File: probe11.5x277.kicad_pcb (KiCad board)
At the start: 2 copper layers, 297 x 11.5 mm, 12 parts, among them J1 CN10, J2 CN10

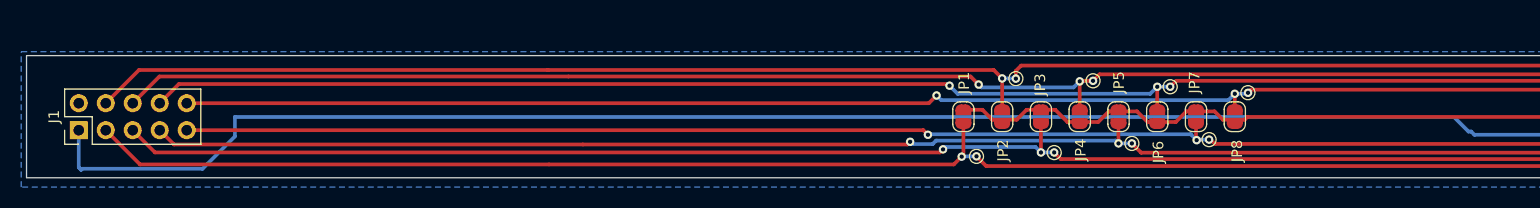
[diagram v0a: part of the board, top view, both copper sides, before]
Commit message: Silkscreen updated
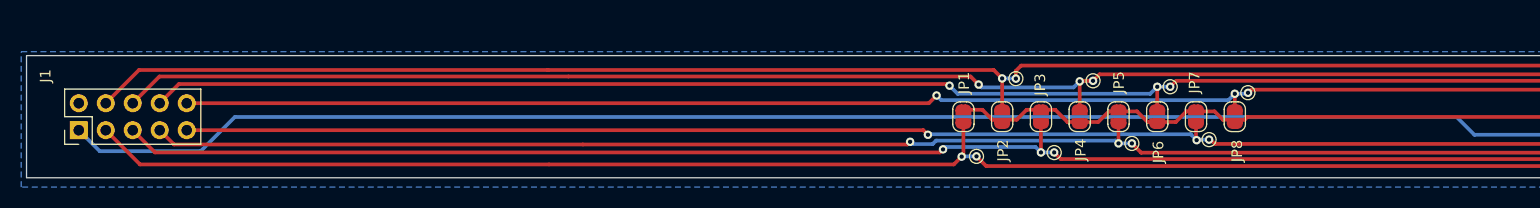
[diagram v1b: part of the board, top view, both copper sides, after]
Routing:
- net Net-(J1-Pin_1): track 288.3 -> 283.8 mm
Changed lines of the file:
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@@
 		(tags "Through hole pin header THT 2x05 2.54mm double row")
 		(property "Reference" "J1"
-			(at 1.27 -2.33 -90)
+			(at 5.1056 -3.1308 -90)
 			(layer "F.SilkS")
 			(effects
@@
 		(layer "F.SilkS")
 	)
+	(gr_text_box "Patento kft.\ntojape@gmail.com"
+		(start 228.7524 97.7392)
+		(end 257.3528 102.1588)
+		(layer "F.SilkS")
+		(effects
+			(font
+				(size 1 1)
+				(thickness 0.1)
+			)
+			(justify top)
+		)
+		(border yes)
+		(stroke
+			(width 0.1)
+			(type solid)
+		)
+	)
+	(gr_text_box "C  1  3  5  7"
+		(start 55.118 102.9716)
+		(end 67.9196 105.0036)
+		(layer "F.SilkS")
+		(effects
+			(font
+				(size 1 1)
+				(thickness 0.1)
+			)
+			(justify left top)
+		)
+		(border yes)
+		(stroke
+			(width 0.1)
+			(type solid)
+		)
+	)
+	(gr_text_box "probe11.5x277"
+		(start 77.8764 98.6028)
+		(end 92.6084 101.346)
+		(layer "F.SilkS")
+		(effects
+			(font
+				(size 1 1)
+				(thickness 0.1)
+			)
+			(justify top)
+		)
+		(border yes)
+		(stroke
+			(width 0.1)
+			(type solid)
+		)
+	)
+	(gr_text_box "C  2  4  6  8"
+		(start 54.9656 94.6912)
+		(end 67.7672 96.7232)
+		(layer "F.SilkS")
+		(effects
+			(font
+				(size 1 1)
+				(thickness 0.1)
+			)
+			(justify left top)
+		)
+		(border yes)
+		(stroke
+			(width 0.1)
+			(type solid)
+		)
+	)
+	(gr_text_box "remote"
+		(start 345.5924 97.2312)
+		(end 348.1324 102.7176)
+		(angle 90)
+		(layer "F.SilkS")
+		(effects
+			(font
+				(size 1 1)
+				(thickness 0.1)
+			)
+			(justify top)
+		)
+		(border yes)
+		(stroke
+			(width 0.1)
+			(type solid)
+		)
+	)
+	(gr_text_box "near"
+		(start 52.1716 97.6884)
+		(end 54.61 102.362)
+		(angle 90)
+		(layer "F.SilkS")
+		(effects
+			(font
+				(size 1 1)
+				(thickness 0.1)
+			)
+			(justify top)
+		)
+		(border yes)
+		(stroke
+			(width 0.1)
+			(type solid)
+		)
+	)
 	(segment
 		(start 147 100.65)
@@
 	)
 	(segment
+		(start 203.23977 101.7016)
+		(end 187.8076 101.7016)
+		(width 0.35)
+		(layer "B.Cu")
+		(net 2)
+	)
+	(segment
 		(start 333.42 100.0252)
 		(end 333.42 101.27)
@@
 	)
 	(segment
-		(start 56.642 105.0036)
-		(end 56.42 104.7816)
+		(start 186.1312 100.0252)
+		(end 71.12 100.0252)
 		(width 0.35)
 		(layer "B.Cu")
@@
 	)
 	(segment
-		(start 56.7436 104.902)
-		(end 56.642 105.0036)
+		(start 203.81 100)
+		(end 333.3948 100)
 		(width 0.35)
 		(layer "B.Cu")
@@
 	)
 	(segment
-		(start 203.81 100)
-		(end 333.3948 100)
+		(start 187.8076 101.7016)
+		(end 186.1312 100.0252)
 		(width 0.35)
 		(layer "B.Cu")
@@
 	)
 	(segment
-		(start 187.2488 101.3968)
-		(end 185.8772 100.0252)
+		(start 203.81 100)
+		(end 203.81 101.13137)
 		(width 0.35)
 		(layer "B.Cu")
@@
 	)
 	(segment
-		(start 203.81 100)
-		(end 203.81 101.13137)
+		(start 333.42 98.73)
+		(end 333.42 100.0252)
 		(width 0.35)
 		(layer "B.Cu")
@@
 	)
 	(segment
-		(start 187.8076 101.7016)
-		(end 187.5028 101.3968)
+		(start 58.3978 103.2478)
+		(end 56.42 101.27)
 		(width 0.35)
 		(layer "B.Cu")
@@
 	)
 	(segment
-		(start 333.42 98.73)
-		(end 333.42 100.0252)
+		(start 67.8974 103.2478)
+		(end 58.3978 103.2478)
 		(width 0.35)
 		(layer "B.Cu")
@@
 	)
 	(segment
-		(start 56.42 104.7816)
-		(end 56.42 101.27)
+		(start 333.3948 100)
+		(end 333.42 100.0252)
 		(width 0.35)
 		(layer "B.Cu")
@@
 	)
 	(segment
-		(start 333.3948 100)
-		(end 333.42 100.0252)
+		(start 203.81 101.13137)
+		(end 203.23977 101.7016)
 		(width 0.35)
 		(layer "B.Cu")
@@
 	)
 	(segment
-		(start 71.12 101.854)
-		(end 68.072 104.902)
+		(start 71.12 100.0252)
+		(end 67.8974 103.2478)
 		(width 0.35)
 		(layer "B.Cu")
-		(net 2)
-	)
-	(segment
-		(start 185.8772 100.0252)
-		(end 71.12 100.0252)
-		(width 0.35)
-		(layer "B.Cu")
-		(net 2)
-	)
-	(segment
-		(start 203.81 101.13137)
-		(end 203.23977 101.7016)
-		(width 0.35)
-		(layer "B.Cu")
-		(net 2)
-	)
-	(segment
-		(start 71.12 100.0252)
-		(end 71.12 101.854)
-		(width 0.35)
-		(layer "B.Cu")
-		(net 2)
-	)
-	(segment
-		(start 187.5028 101.3968)
-		(end 187.2488 101.3968)
-		(width 0.35)
-		(layer "B.Cu")
-		(net 2)
-	)
-	(segment
-		(start 68.072 104.902)
-		(end 56.7436 104.902)
-		(width 0.35)
-		(layer "B.Cu")
-		(net 2)
-	)
-	(segment
-		(start 203.23977 101.7016)
-		(end 187.8076 101.7016)
-		(width 0.35)
-		(layer "B.Cu")

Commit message: Updated before manufacturing
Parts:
- J1, J2: footprint Connector_PinHeader_2.54mm:PinHeader_2x05_P2.54mm_Vertical -> Library:PinHeader_2x05_P2.54mm_Vertical
- JP1, JP2, JP3, JP4, JP5, JP6, JP7, JP8: footprint Jumper:SolderJumper-2_P1.3mm_Open_RoundedPad1.0x1.5mm -> Library:SolderJumper-2_P1.3mm_Open_RoundedPad1.0x1.5mm
- PCB1: footprint TJP_LIB:PCB11x297 -> Library:PCB11x297
- TH1: footprint TJP_LIB:NTC_5x2 -> Library:NTC_5x2
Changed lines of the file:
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@@
 	(net 9 "Net-(J1-Pin_4)")
 	(net 10 "Net-(J1-Pin_10)")
-	(footprint "Jumper:SolderJumper-2_P1.3mm_Open_RoundedPad1.0x1.5mm"
+	(footprint "Library:SolderJumper-2_P1.3mm_Open_RoundedPad1.0x1.5mm"
 		(layer "F.Cu")
 		(at 139.7 100 90)
@@
 			)
 		)
-		(property "Footprint" "Jumper:SolderJumper-2_P1.3mm_Open_RoundedPad1.0x1.5mm"
+		(property "Footprint" "Library:SolderJumper-2_P1.3mm_Open_RoundedPad1.0x1.5mm"
 			(at 0 0 90)
 			(unlocked yes)
@@
 		)
 	)
-	(footprint "Jumper:SolderJumper-2_P1.3mm_Open_RoundedPad1.0x1.5mm"
+	(footprint "Library:SolderJumper-2_P1.3mm_Open_RoundedPad1.0x1.5mm"
 		(layer "F.Cu")
 		(at 165.25 100 -90)
@@
 			)
 		)
-		(property "Footprint" "Jumper:SolderJumper-2_P1.3mm_Open_RoundedPad1.0x1.5mm"
+		(property "Footprint" "Library:SolderJumper-2_P1.3mm_Open_RoundedPad1.0x1.5mm"
 			(at 0 0 -90)
 			(unlocked yes)
@@
 		)
 	)
-	(footprint "Jumper:SolderJumper-2_P1.3mm_Open_RoundedPad1.0x1.5mm"
+	(footprint "Library:SolderJumper-2_P1.3mm_Open_RoundedPad1.0x1.5mm"
 		(layer "F.Cu")
 		(at 147 100 90)
@@
 			)
 		)
-		(property "Footprint" "Jumper:SolderJumper-2_P1.3mm_Open_RoundedPad1.0x1.5mm"
+		(property "Footprint" "Library:SolderJumper-2_P1.3mm_Open_RoundedPad1.0x1.5mm"
 			(at 0 0 90)
 			(unlocked yes)
@@
 		)
 	)
-	(footprint "Jumper:SolderJumper-2_P1.3mm_Open_RoundedPad1.0x1.5mm"
+	(footprint "Library:SolderJumper-2_P1.3mm_Open_RoundedPad1.0x1.5mm"
 		(layer "F.Cu")
 		(at 143.35 100 -90)
@@
 			)
 		)
-		(property "Footprint" "Jumper:SolderJumper-2_P1.3mm_Open_RoundedPad1.0x1.5mm"
+		(property "Footprint" "Library:SolderJumper-2_P1.3mm_Open_RoundedPad1.0x1.5mm"
 			(at 0 0 -90)
 			(unlocked yes)
@@
 		)
 	)
-	(footprint "Jumper:SolderJumper-2_P1.3mm_Open_RoundedPad1.0x1.5mm"
+	(footprint "Library:SolderJumper-2_P1.3mm_Open_RoundedPad1.0x1.5mm"
 		(layer "F.Cu")
 		(at 154.3 100 90)
@@
 			)
 		)
-		(property "Footprint" "Jumper:SolderJumper-2_P1.3mm_Open_RoundedPad1.0x1.5mm"
+		(property "Footprint" "Library:SolderJumper-2_P1.3mm_Open_RoundedPad1.0x1.5mm"
 			(at 0 0 90)
 			(unlocked yes)
@@
 		)
 	)
-	(footprint "Jumper:SolderJumper-2_P1.3mm_Open_RoundedPad1.0x1.5mm"
+	(footprint "Library:SolderJumper-2_P1.3mm_Open_RoundedPad1.0x1.5mm"
 		(layer "F.Cu")
 		(at 161.6 100 90)
@@
 			)
 		)
-		(property "Footprint" "Jumper:SolderJumper-2_P1.3mm_Open_RoundedPad1.0x1.5mm"
+		(property "Footprint" "Library:SolderJumper-2_P1.3mm_Open_RoundedPad1.0x1.5mm"
 			(at 0 0 90)
 			(unlocked yes)
@@
 		)
 	)
-	(footprint "Connector_PinHeader_2.54mm:PinHeader_2x05_P2.54mm_Vertical"
+	(footprint "Library:PinHeader_2x05_P2.54mm_Vertical"
 		(layer "F.Cu")
 		(at 56.42 101.27 90)
@@
 			)
 		)
-		(property "Footprint" "Connector_PinHeader_2.54mm:PinHeader_2x05_P2.54mm_Vertical"
+		(property "Footprint" "Library:PinHeader_2x05_P2.54mm_Vertical"
 			(at 0 0 90)
 			(unlocked yes)
@@
 			(pintype "passive")
 		)
-		(model "${KICAD8_3DMODEL_DIR}/Connector_PinHeader_2.54mm.3dshapes/PinHeader_2x05_P2.54mm_Vertical.wrl"
+		(model "${KIPRJMOD}/packages3D/PinHeader_2x05_P2.54mm_Vertical.wrl"
 			(offset
 				(xyz 0 0 0)
@@
 		)
 	)
-	(footprint "TJP_LIB:NTC_5x2"
+	(footprint "Library:NTC_5x2"
 		(layer "F.Cu")
 		(at 200 100)
@@
 			)
 		)
-		(property "Footprint" "TJP_LIB:NTC_5x2"
+		(property "Footprint" "Library:NTC_5x2"
 			(at 0 0 0)
 			(unlocked yes)
@@
 			(pintype "passive")
 		)
-		(model "${KICAD8_3DMODEL_DIR}/Diode_THT.3dshapes/D_DO-35_SOD27_P7.62mm_Horizontal.wrl"
+		(model "${KIPRJMOD}/packages3D/D_DO-35_SOD27_P7.62mm_Horizontal.wrl"
 			(offset
 				(xyz -3.81 0 -1.2)
@@
 		)
 	)
-	(footprint "TJP_LIB:PCB11x297"
+	(footprint "Library:PCB11x297"
 		(layer "F.Cu")
 		(at 200 100)
@@
 			)
 		)
-		(property "Footprint" "TJP_LIB:PCB11x297"
+		(property "Footprint" "Library:PCB11x297"
 			(at 0 -10.5 0)
 			(unlocked yes)
@@
 		)
 	)
-	(footprint "Jumper:SolderJumper-2_P1.3mm_Open_RoundedPad1.0x1.5mm"
+	(footprint "Library:SolderJumper-2_P1.3mm_Open_RoundedPad1.0x1.5mm"
 		(layer "F.Cu")
 		(at 157.95 100 -90)
@@
 			)
 		)
-		(property "Footprint" "Jumper:SolderJumper-2_P1.3mm_Open_RoundedPad1.0x1.5mm"
+		(property "Footprint" "Library:SolderJumper-2_P1.3mm_Open_RoundedPad1.0x1.5mm"
 			(at 0 0 -90)
 			(unlocked yes)
@@
 		)
 	)
-	(footprint "Jumper:SolderJumper-2_P1.3mm_Open_RoundedPad1.0x1.5mm"
+	(footprint "Library:SolderJumper-2_P1.3mm_Open_RoundedPad1.0x1.5mm"
 		(layer "F.Cu")
 		(at 150.65 100 -90)
@@
 			)
 		)
-		(property "Footprint" "Jumper:SolderJumper-2_P1.3mm_Open_RoundedPad1.0x1.5mm"
+		(property "Footprint" "Library:SolderJumper-2_P1.3mm_Open_RoundedPad1.0x1.5mm"
 			(at 0 0 -90)
 			(unlocked yes)
@@
 		)
 	)
-	(footprint "Connector_PinHeader_2.54mm:PinHeader_2x05_P2.54mm_Vertical"
+	(footprint "Library:PinHeader_2x05_P2.54mm_Vertical"
 		(layer "F.Cu")
 		(at 333.42 101.27 90)
@@
 			)
 		)
-		(property "Footprint" "Connector_PinHeader_2.54mm:PinHeader_2x05_P2.54mm_Vertical"
+		(property "Footprint" "Library:PinHeader_2x05_P2.54mm_Vertical"
 			(at 0 0 90)
 			(unlocked yes)
@@
 			(pintype "passive")
 		)
-		(model "${KICAD8_3DMODEL_DIR}/Connector_PinHeader_2.54mm.3dshapes/PinHeader_2x05_P2.54mm_Vertical.wrl"
+		(model "${KIPRJMOD}/packages3D/PinHeader_2x05_P2.54mm_Vertical.wrl"
 			(offset
 				(xyz 0 0 0)
